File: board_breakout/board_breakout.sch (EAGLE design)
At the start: 3 parts

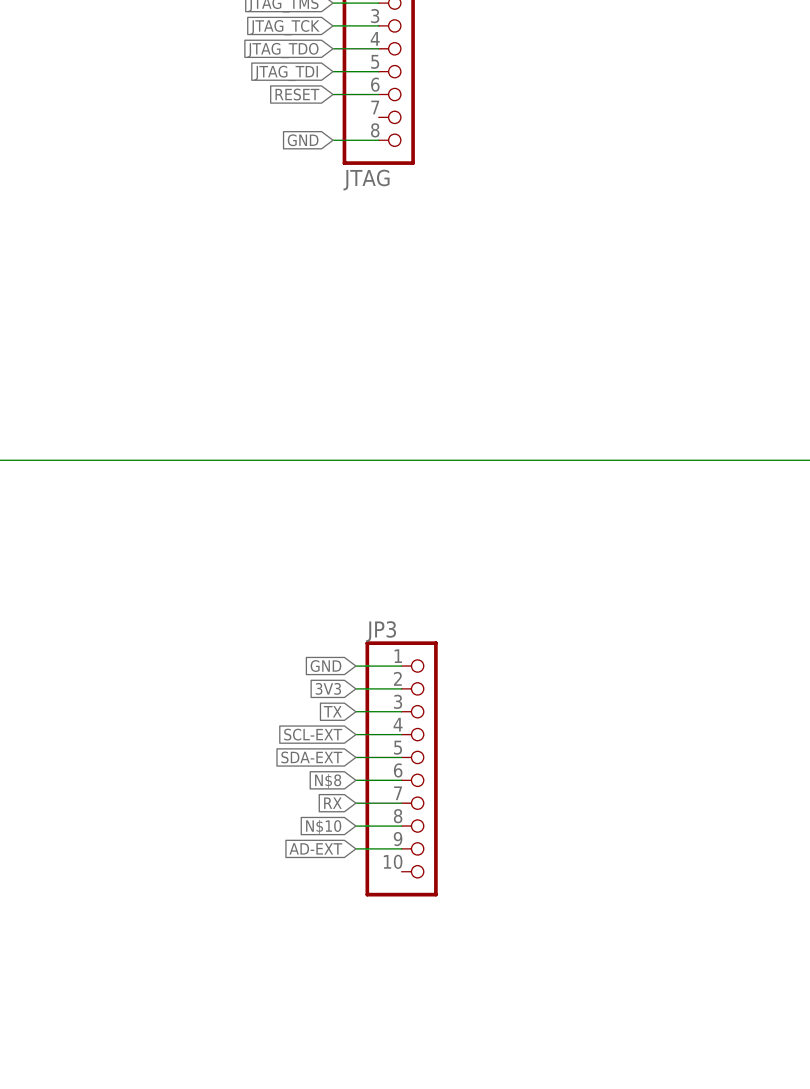
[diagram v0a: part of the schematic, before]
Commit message: breakout board now one-sided
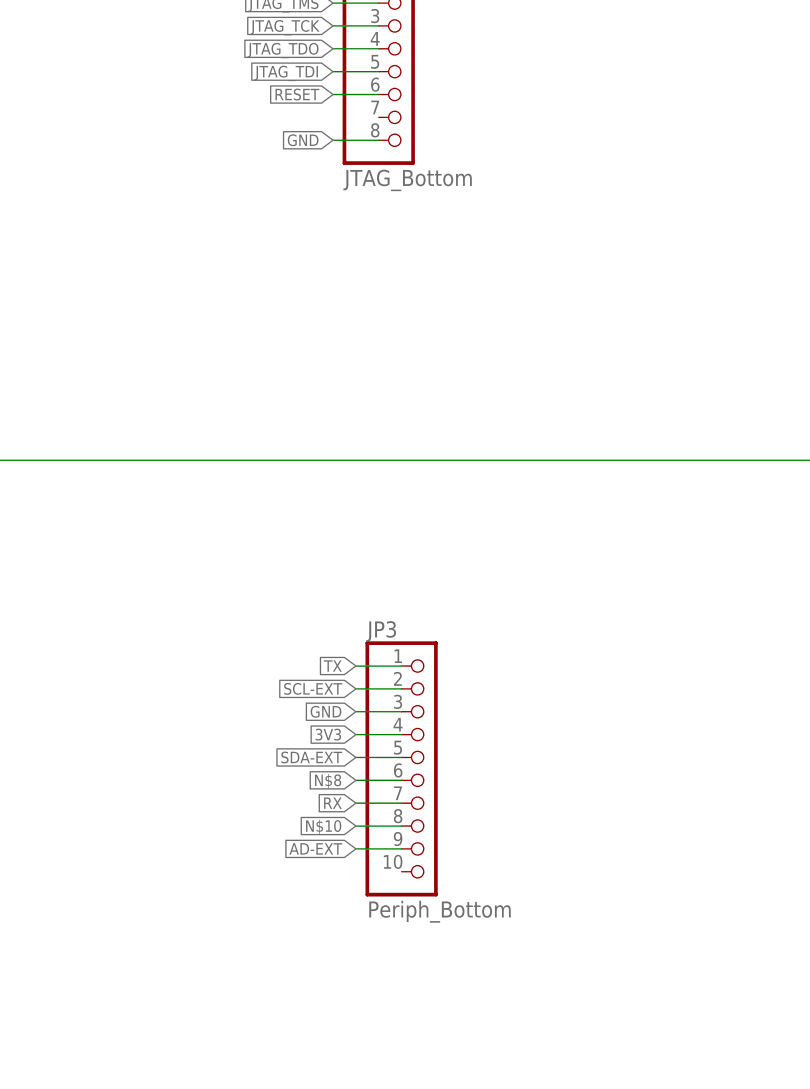
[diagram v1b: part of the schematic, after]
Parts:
- JP2: value JTAG -> JTAG_Bottom
- JP3: value (none) -> Periph_Bottom
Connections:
- net 3V3: now also JP3.4; no longer JP3.2
- net GND: now also JP3.3; no longer JP3.1
- net SCL-EXT: now also JP3.2; no longer JP3.4
- net TX: now also JP3.1; no longer JP3.3
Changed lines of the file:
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@@
 <part name="P+1" library="supply1" deviceset="VCC" device=""/>
 <part name="GND1" library="supply1" deviceset="GND" device=""/>
-<part name="JP2" library="pinhead" deviceset="PINHD-1X8" device="" value="JTAG"/>
-<part name="JP3" library="pinhead" deviceset="PINHD-1X10" device=""/>
+<part name="JP2" library="pinhead" deviceset="PINHD-1X8" device="" value="JTAG_Bottom"/>
+<part name="JP3" library="pinhead" deviceset="PINHD-1X10" device="" value="Periph_Bottom"/>
 </parts>
 <sheets>
@@
 </segment>
 <segment>
-<pinref part="JP3" gate="A" pin="2"/>
-<wire x1="203.2" y1="63.5" x2="198.12" y2="63.5" width="0.1524" layer="91"/>
-<label x="198.12" y="63.5" size="1.27" layer="95" rot="MR0" xref="yes"/>
+<pinref part="JP3" gate="A" pin="4"/>
+<wire x1="203.2" y1="58.42" x2="198.12" y2="58.42" width="0.1524" layer="91"/>
+<label x="198.12" y="58.42" size="1.27" layer="95" rot="MR0" xref="yes"/>
 </segment>
 </net>
@@
 </segment>
 <segment>
-<pinref part="JP3" gate="A" pin="1"/>
-<wire x1="203.2" y1="66.04" x2="198.12" y2="66.04" width="0.1524" layer="91"/>
-<label x="198.12" y="66.04" size="1.27" layer="95" rot="MR0" xref="yes"/>
+<pinref part="JP3" gate="A" pin="3"/>
+<wire x1="203.2" y1="60.96" x2="198.12" y2="60.96" width="0.1524" layer="91"/>
+<label x="198.12" y="60.96" size="1.27" layer="95" rot="MR0" xref="yes"/>
 </segment>
 </net>
@@
 </segment>
 <segment>
-<pinref part="JP3" gate="A" pin="3"/>
-<wire x1="203.2" y1="60.96" x2="198.12" y2="60.96" width="0.1524" layer="91"/>
-<label x="198.12" y="60.96" size="1.27" layer="95" rot="MR0" xref="yes"/>
+<pinref part="JP3" gate="A" pin="1"/>
+<wire x1="203.2" y1="66.04" x2="198.12" y2="66.04" width="0.1524" layer="91"/>
+<label x="198.12" y="66.04" size="1.27" layer="95" rot="MR0" xref="yes"/>
 </segment>
 </net>
@@
 </segment>
 <segment>
-<pinref part="JP3" gate="A" pin="4"/>
-<wire x1="203.2" y1="58.42" x2="198.12" y2="58.42" width="0.1524" layer="91"/>
-<label x="198.12" y="58.42" size="1.27" layer="95" rot="MR0" xref="yes"/>
+<pinref part="JP3" gate="A" pin="2"/>
+<wire x1="203.2" y1="63.5" x2="198.12" y2="63.5" width="0.1524" layer="91"/>
+<label x="198.12" y="63.5" size="1.27" layer="95" rot="MR0" xref="yes"/>
 </segment>
 </net>

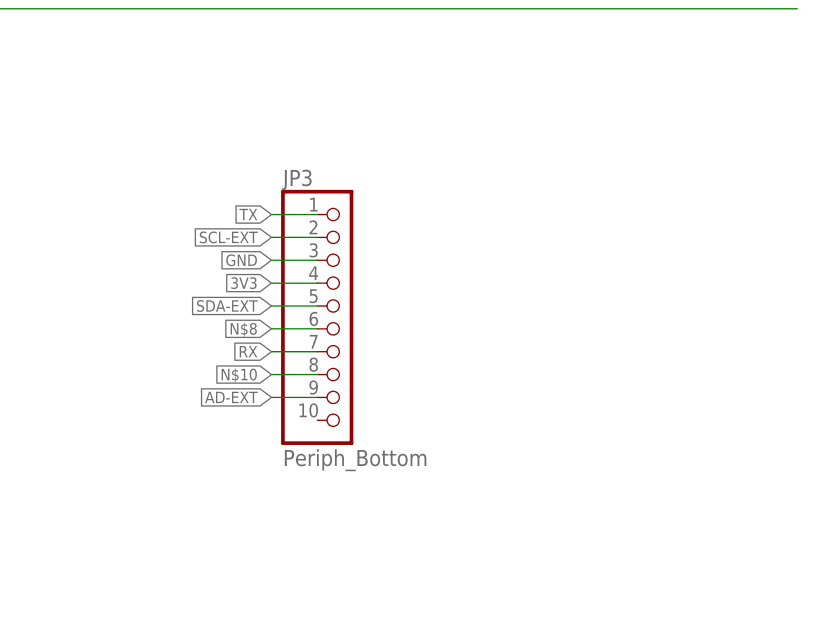
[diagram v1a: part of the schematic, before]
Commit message: breakout board added header
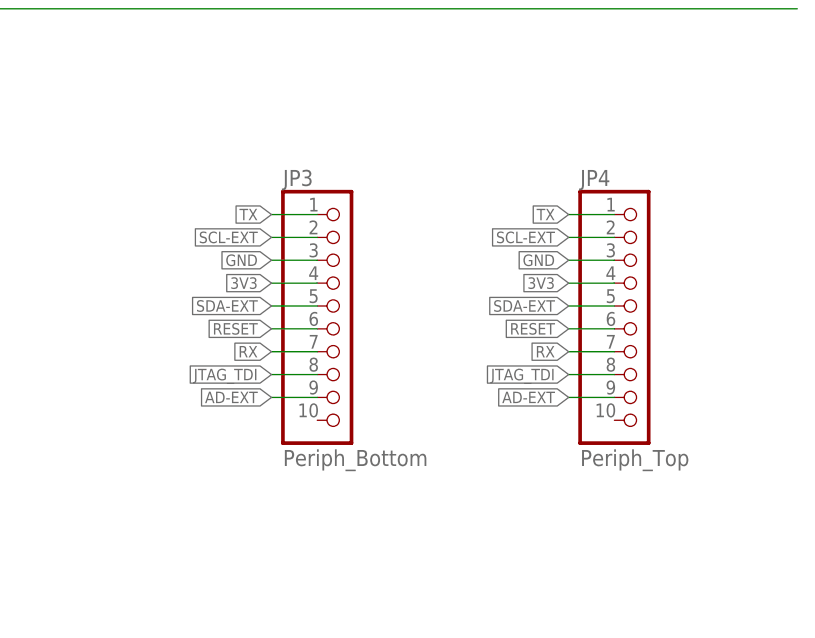
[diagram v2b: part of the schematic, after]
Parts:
- added JP4: Periph_Top, microbuilder:HEADER-1X10SMT
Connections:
- removed net N$10: JP3.8
- removed net N$8: JP3.6
- net 3V3: now also JP4.4
- net AD-EXT: now also JP4.9
- net GND: now also JP4.3
- net JTAG_TDI: now also JP3.8, JP4.8
- net RESET: now also JP3.6, JP4.6
- net RX: now also JP4.7
- net SCL-EXT: now also JP4.2
- net SDA-EXT: now also JP4.5
- net TX: now also JP4.1
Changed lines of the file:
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@@
 <layer number="48" name="Document" color="7" fill="1" visible="no" active="no"/>
 <layer number="49" name="Reference" color="7" fill="1" visible="no" active="no"/>
+<layer number="50" name="dxf" color="7" fill="1" visible="no" active="no"/>
 <layer number="51" name="tDocu" color="7" fill="1" visible="no" active="no"/>
 <layer number="52" name="bDocu" color="7" fill="1" visible="no" active="no"/>
+<layer number="53" name="tGND_GNDA" color="7" fill="9" visible="no" active="no"/>
+<layer number="54" name="bGND_GNDA" color="1" fill="9" visible="no" active="no"/>
+<layer number="56" name="wert" color="7" fill="1" visible="no" active="no"/>
 <layer number="91" name="Nets" color="2" fill="1" visible="yes" active="yes"/>
 <layer number="92" name="Busses" color="1" fill="1" visible="yes" active="yes"/>
@@
 <layer number="97" name="Info" color="7" fill="1" visible="yes" active="yes"/>
 <layer number="98" name="Guide" color="6" fill="1" visible="yes" active="yes"/>
+<layer number="100" name="Muster" color="7" fill="1" visible="yes" active="yes"/>
+<layer number="101" name="Patch_Top" color="12" fill="4" visible="yes" active="yes"/>
+<layer number="102" name="Mittellin" color="7" fill="1" visible="yes" active="yes"/>
+<layer number="103" name="Stiffner" color="7" fill="1" visible="yes" active="yes"/>
+<layer number="104" name="Name" color="7" fill="1" visible="yes" active="yes"/>
+<layer number="105" name="Beschreib" color="7" fill="1" visible="yes" active="yes"/>
+<layer number="106" name="BGA-Top" color="7" fill="1" visible="yes" active="yes"/>
+<layer number="107" name="BD-Top" color="7" fill="1" visible="yes" active="yes"/>
+<layer number="108" name="tBridges" color="7" fill="1" visible="yes" active="yes"/>
+<layer number="109" name="tBPL" color="7" fill="1" visible="yes" active="yes"/>
+<layer number="110" name="bBPL" color="7" fill="1" visible="yes" active="yes"/>
+<layer number="111" name="MPL" color="7" fill="1" visible="yes" active="yes"/>
+<layer number="112" name="tSilk" color="7" fill="1" visible="yes" active="yes"/>
+<layer number="121" name="sName" color="7" fill="1" visible="yes" active="yes"/>
+<layer number="122" name="_bPlace" color="7" fill="1" visible="yes" active="yes"/>
+<layer number="125" name="_tNames" color="7" fill="1" visible="yes" active="yes"/>
+<layer number="126" name="_bNames" color="7" fill="1" visible="yes" active="yes"/>
+<layer number="127" name="_tValues" color="7" fill="1" visible="yes" active="yes"/>
+<layer number="128" name="_bValues" color="7" fill="1" visible="yes" active="yes"/>
+<layer number="144" name="Drill_legend" color="7" fill="1" visible="yes" active="yes"/>
+<layer number="151" name="HeatSink" color="7" fill="1" visible="yes" active="yes"/>
+<layer number="152" name="_bDocu" color="7" fill="1" visible="yes" active="yes"/>
+<layer number="200" name="200bmp" color="1" fill="10" visible="yes" active="yes"/>
+<layer number="201" name="201bmp" color="7" fill="1" visible="yes" active="yes"/>
+<layer number="202" name="202bmp" color="7" fill="1" visible="yes" active="yes"/>
+<layer number="203" name="203bmp" color="7" fill="1" visible="yes" active="yes"/>
+<layer number="204" name="204bmp" color="7" fill="1" visible="yes" active="yes"/>
+<layer number="205" name="205bmp" color="7" fill="1" visible="yes" active="yes"/>
+<layer number="248" name="Housing" color="7" fill="1" visible="yes" active="yes"/>
+<layer number="249" name="Edge" color="7" fill="1" visible="yes" active="yes"/>
+<layer number="250" name="Descript" color="7" fill="1" visible="yes" active="yes"/>
+<layer number="251" name="SMDround" color="7" fill="1" visible="yes" active="yes"/>
+<layer number="254" name="cooling" color="7" fill="1" visible="yes" active="yes"/>
 </layers>
 <schematic xreflabel="%F%N/%S.%C%R" xrefpart="/%S.%C%R">
@@
 <part name="JP2" library="pinhead" deviceset="PINHD-1X8" device="" value="JTAG_Bottom"/>
 <part name="JP3" library="pinhead" deviceset="PINHD-1X10" device="" value="Periph_Bottom"/>
+<part name="JP4" library="microbuilder" deviceset="HEADER-1X10" device="SMT" value="Periph_Top"/>
 </parts>
 <sheets>
@@
 <instance part="JP2" gate="A" x="203.2" y="132.08"/>
 <instance part="JP3" gate="A" x="205.74" y="55.88"/>
+<instance part="JP4" gate="A" x="238.76" y="55.88"/>
 </instances>
 <busses>
@@
 <label x="198.12" y="58.42" size="1.27" layer="95" rot="MR0" xref="yes"/>
 </segment>
+<segment>
+<label x="231.14" y="58.42" size="1.27" layer="95" rot="MR0" xref="yes"/>
+<pinref part="JP4" gate="A" pin="4"/>
+<wire x1="236.22" y1="58.42" x2="231.14" y2="58.42" width="0.1524" layer="91"/>
+</segment>
 </net>
 <net name="GND" class="0">
@@
 <label x="198.12" y="60.96" size="1.27" layer="95" rot="MR0" xref="yes"/>
 </segment>
+<segment>
+<label x="231.14" y="60.96" size="1.27" layer="95" rot="MR0" xref="yes"/>
+<pinref part="JP4" gate="A" pin="3"/>
+<wire x1="231.14" y1="60.96" x2="236.22" y2="60.96" width="0.1524" layer="91"/>
+</segment>
 </net>
 <net name="TX" class="0">
@@
 <label x="198.12" y="66.04" size="1.27" layer="95" rot="MR0" xref="yes"/>
 </segment>
+<segment>
+<label x="231.14" y="66.04" size="1.27" layer="95" rot="MR0" xref="yes"/>
+<pinref part="JP4" gate="A" pin="1"/>
+<wire x1="236.22" y1="66.04" x2="231.14" y2="66.04" width="0.1524" layer="91"/>
+</segment>
 </net>
 <net name="JTAG_TDO" class="0">
@@
 <label x="198.12" y="45.72" size="1.27" layer="95" rot="MR0" xref="yes"/>
 </segment>
+<segment>
+<label x="231.14" y="45.72" size="1.27" layer="95" rot="MR0" xref="yes"/>
+<pinref part="JP4" gate="A" pin="9"/>
+<wire x1="231.14" y1="45.72" x2="236.22" y2="45.72" width="0.1524" layer="91"/>
+</segment>
 </net>
 <net name="JTAG_TDI" class="0">
@@
 <label x="195.58" y="132.08" size="1.27" layer="95" rot="MR0" xref="yes"/>
 </segment>
+<segment>
+<pinref part="JP3" gate="A" pin="8"/>
+<wire x1="203.2" y1="48.26" x2="198.12" y2="48.26" width="0.1524" layer="91"/>
+<label x="198.12" y="48.26" size="1.27" layer="95" rot="MR0" xref="yes"/>
+</segment>
+<segment>
+<label x="231.14" y="48.26" size="1.27" layer="95" rot="MR0" xref="yes"/>
+<pinref part="JP4" gate="A" pin="8"/>
+<wire x1="236.22" y1="48.26" x2="231.14" y2="48.26" width="0.1524" layer="91"/>
+</segment>
 </net>
 <net name="RX" class="0">
@@
 <label x="198.12" y="50.8" size="1.27" layer="95" rot="MR0" xref="yes"/>
 </segment>
+<segment>
+<label x="231.14" y="50.8" size="1.27" layer="95" rot="MR0" xref="yes"/>
+<pinref part="JP4" gate="A" pin="7"/>
+<wire x1="231.14" y1="50.8" x2="236.22" y2="50.8" width="0.1524" layer="91"/>
+</segment>
 </net>
 <net name="RESET" class="0">
@@
 <label x="195.58" y="129.54" size="1.27" layer="95" rot="MR0" xref="yes"/>
 </segment>
+<segment>
+<pinref part="JP3" gate="A" pin="6"/>
+<wire x1="203.2" y1="53.34" x2="198.12" y2="53.34" width="0.1524" layer="91"/>
+<label x="198.12" y="53.34" size="1.27" layer="95" rot="MR0" xref="yes"/>
+</segment>
+<segment>
+<label x="231.14" y="53.34" size="1.27" layer="95" rot="MR0" xref="yes"/>
+<pinref part="JP4" gate="A" pin="6"/>
+<wire x1="236.22" y1="53.34" x2="231.14" y2="53.34" width="0.1524" layer="91"/>
+</segment>
 </net>
 <net name="N$1" class="0">
@@
 <label x="198.12" y="55.88" size="1.27" layer="95" rot="MR0" xref="yes"/>
 </segment>
+<segment>
+<label x="231.14" y="55.88" size="1.27" layer="95" rot="MR0" xref="yes"/>
+<pinref part="JP4" gate="A" pin="5"/>
+<wire x1="231.14" y1="55.88" x2="236.22" y2="55.88" width="0.1524" layer="91"/>
+</segment>
 </net>
 <net name="SCL-EXT" class="0">
@@
 <label x="198.12" y="63.5" size="1.27" layer="95" rot="MR0" xref="yes"/>
 </segment>
-</net>
-<net name="N$8" class="0">
-<segment>
-<pinref part="JP3" gate="A" pin="6"/>
-<wire x1="203.2" y1="53.34" x2="198.12" y2="53.34" width="0.1524" layer="91"/>
-<label x="198.12" y="53.34" size="1.27" layer="95" rot="MR0" xref="yes"/>
-</segment>
-</net>
-<net name="N$10" class="0">
-<segment>
-<pinref part="JP3" gate="A" pin="8"/>
-<wire x1="203.2" y1="48.26" x2="198.12" y2="48.26" width="0.1524" layer="91"/>
-<label x="198.12" y="48.26" size="1.27" layer="95" rot="MR0" xref="yes"/>
-</segment>
-</net>
+<segment>
+<label x="231.14" y="63.5" size="1.27" layer="95" rot="MR0" xref="yes"/>
+<pinref part="JP4" gate="A" pin="2"/>
+<wire x1="231.14" y1="63.5" x2="236.22" y2="63.5" width="0.1524" layer="91"/>
+</segment>
+</net>
